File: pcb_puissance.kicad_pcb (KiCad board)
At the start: 2 copper layers, 126.5 x 120.5 mm, 32 parts, among them J1 1755736, J10 Conn_01x02, J11 Conn_01x02, J2 1755736, J3 1755736, J4 1755736, J5 1755736, J6 1755736, J7 1755736, J8 1755736, J9 Conn_01x02, K1 SRD-05VDC-SL-C

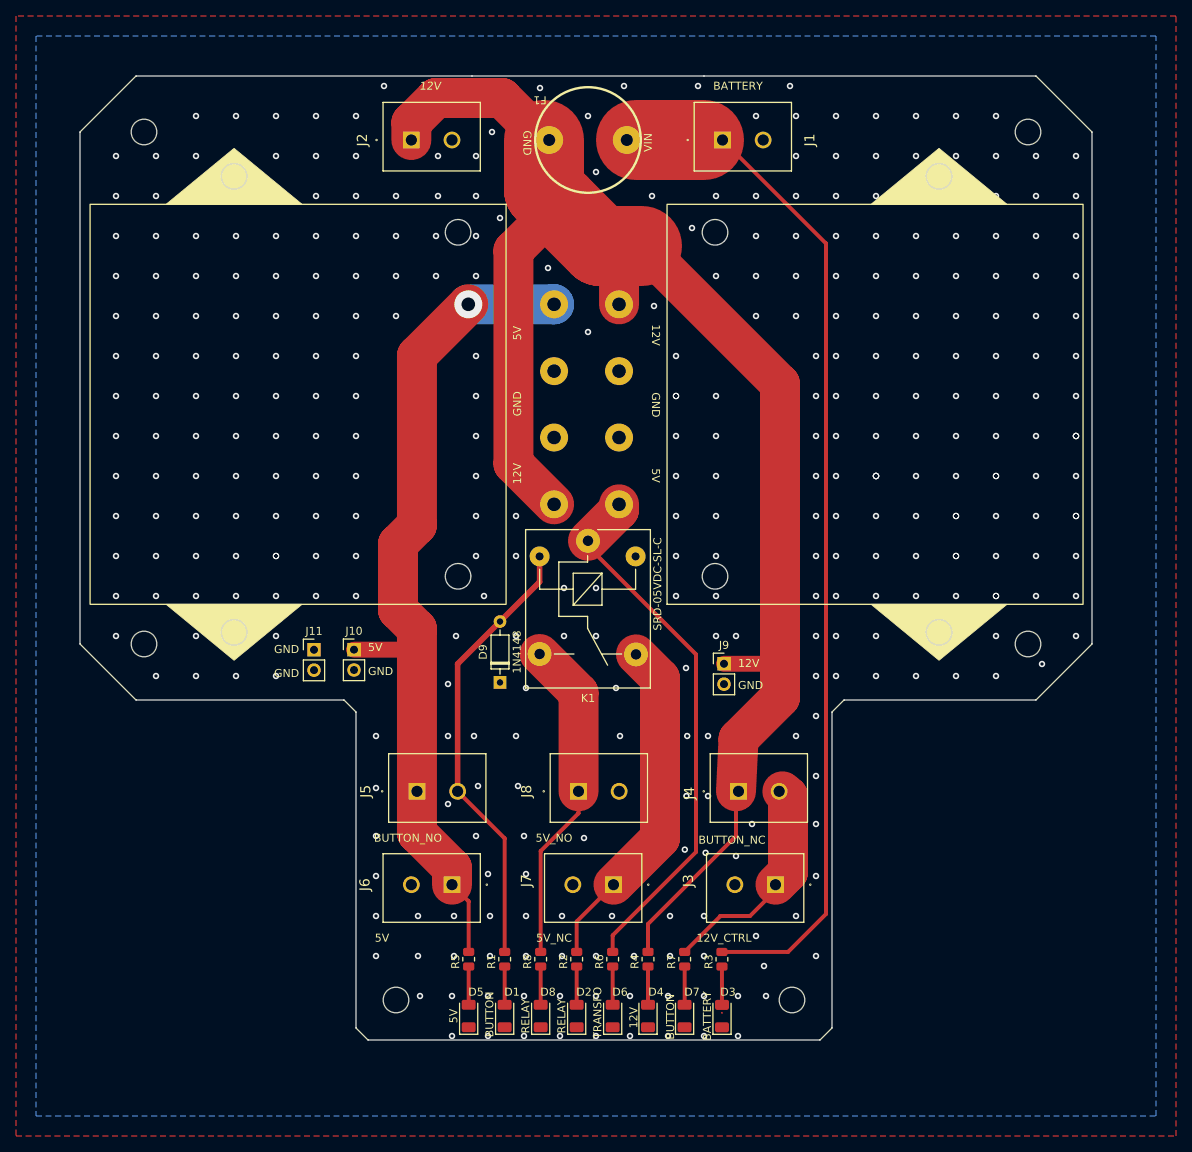
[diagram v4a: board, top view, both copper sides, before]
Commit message: Vias dans les pastilles + textes cachés par les connecteurs
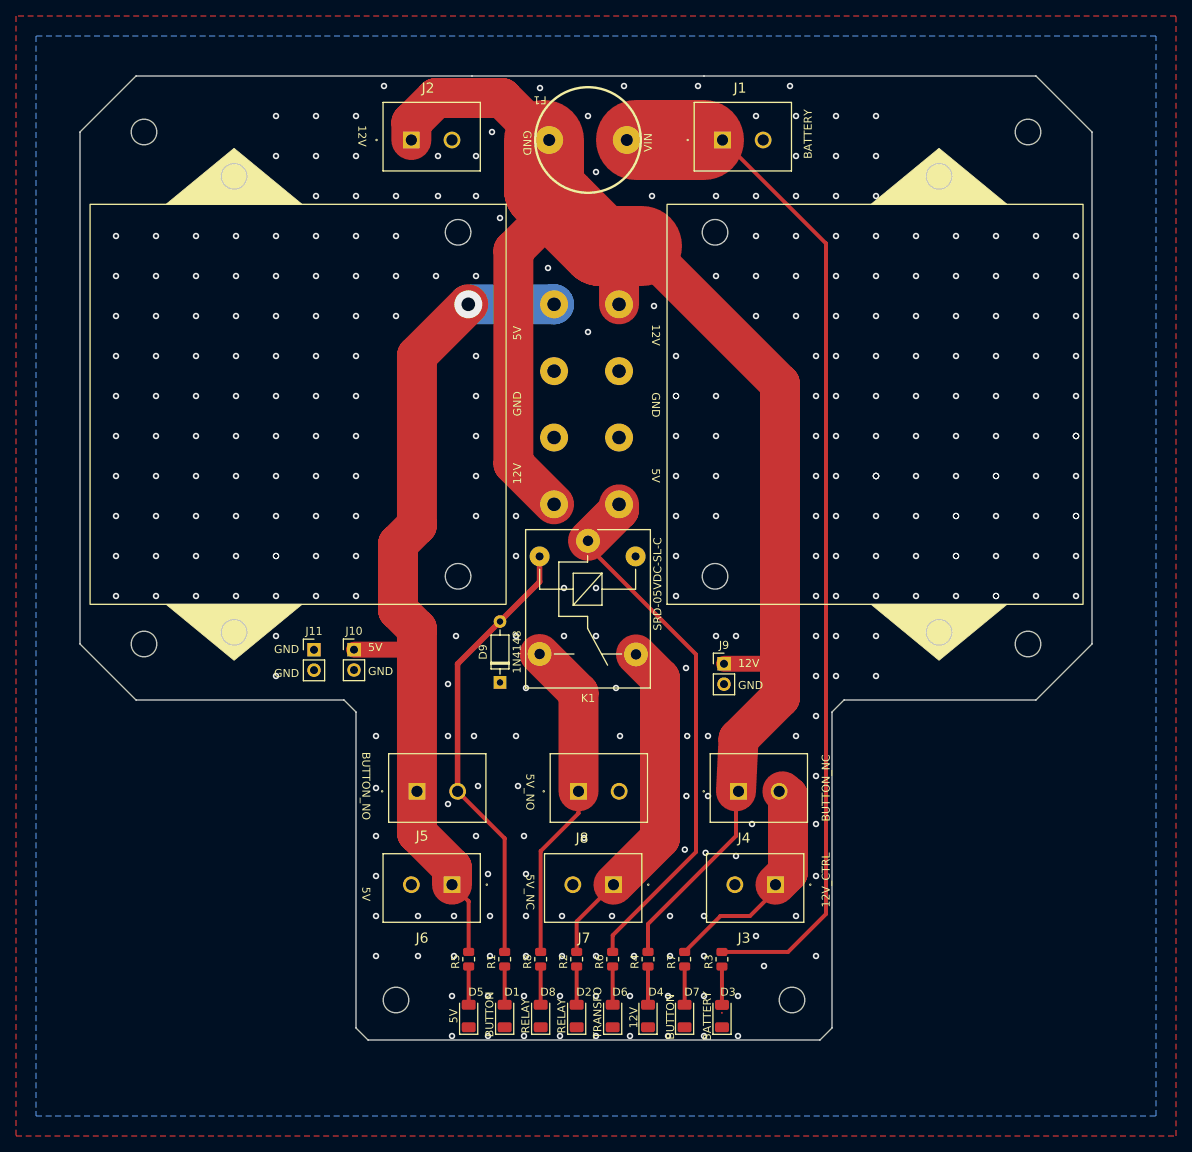
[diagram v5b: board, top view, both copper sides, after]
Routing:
- net GND: vias 361 -> 318

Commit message: Fixations
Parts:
- added Fix1: ~, Library:FIX3.2P7.5, F.Cu at (28.5, 32.0)
- added Fix2: ~, Library:FIX3.2P7.5, F.Cu at (139.0, 32.0)
- added Fix3: ~, Library:FIX3.2P7.5, F.Cu at (28.5, 96.0)
- added Fix4: ~, Library:FIX3.2P7.5, F.Cu at (139.0, 96.0)
- added Fix5: ~, Library:FIX3.2P7.5, F.Cu at (60.0, 140.5)
- added Fix6: ~, Library:FIX3.2P7.5, F.Cu at (109.5, 140.5)
- moved TRANSFO2 0.06 mm to (48.2, 66.0)
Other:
- outline, holes or cut-outs redrawn

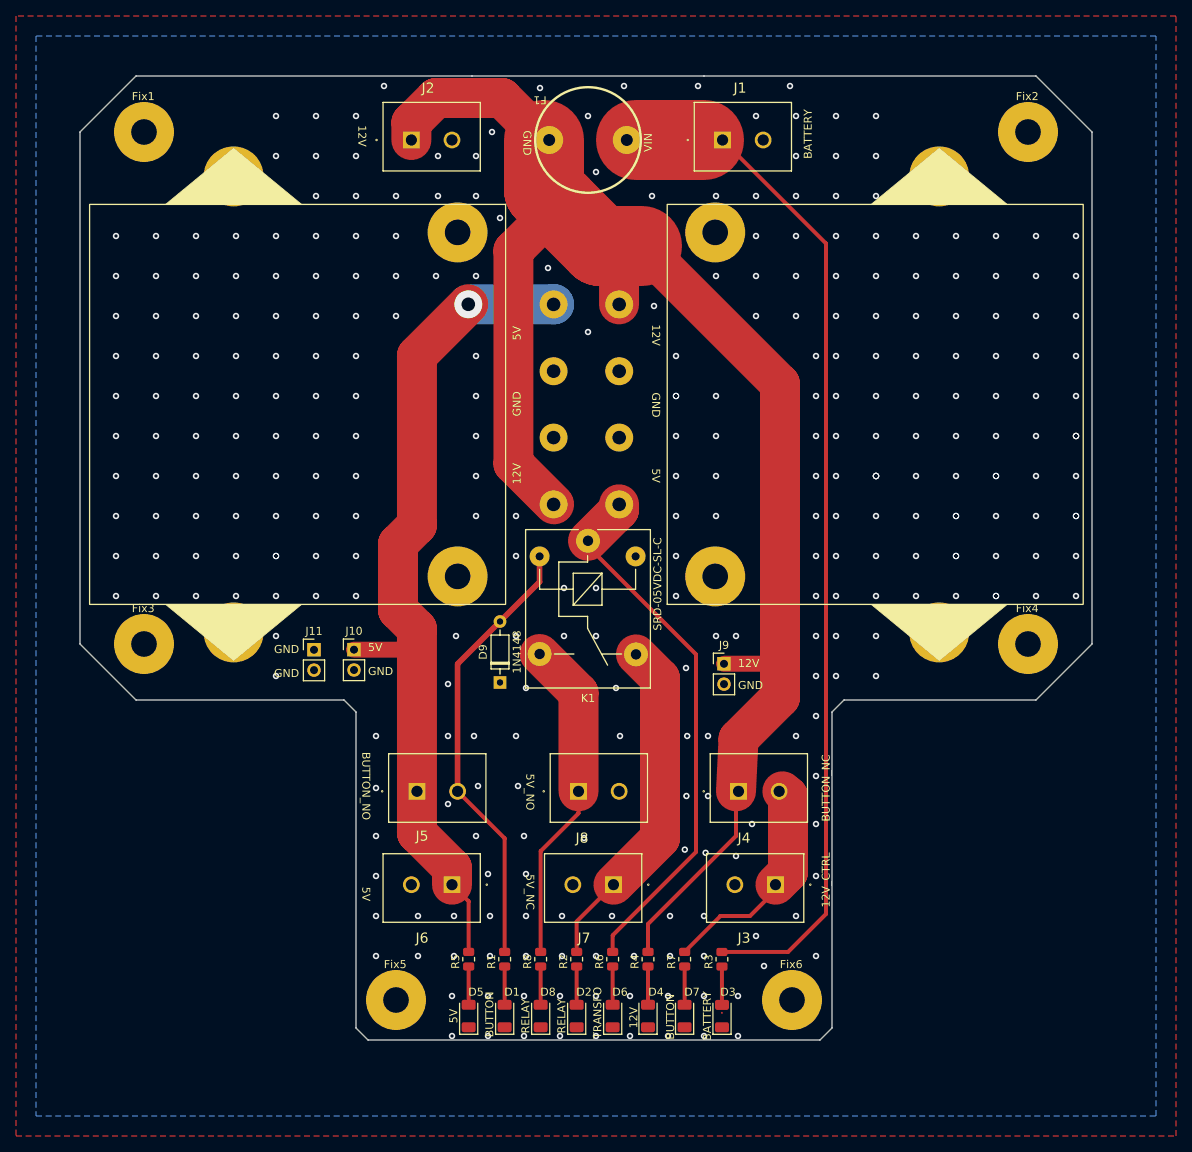
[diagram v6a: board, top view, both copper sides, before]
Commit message: DRC, nettoyage pistes cachées, ajout logos
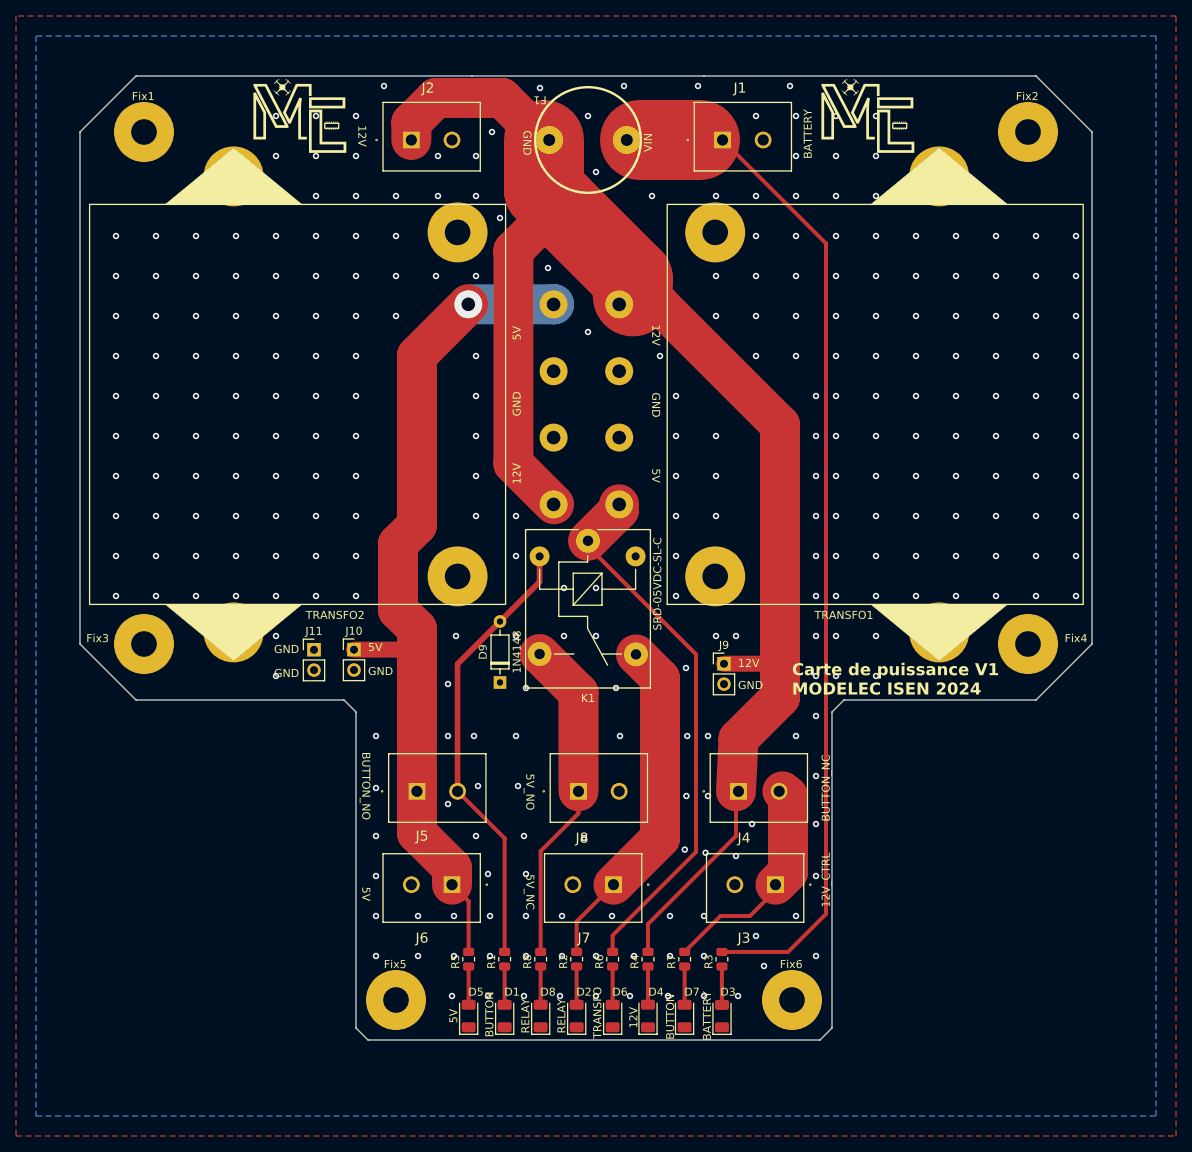
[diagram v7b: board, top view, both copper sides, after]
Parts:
- added G***: LOGO, Library:logo_modelec, F.Cu at (48.0, 30.0)
- added G***: LOGO, Library:logo_modelec, F.Cu at (119.0, 30.0)
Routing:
- net +12V: track 207.9 -> 196.9 mm
- net BATTERY: track 127.0 -> 124.6 mm
- net BUTTON_NC: track 27.9 -> 27.2 mm
- net GND: track 0.01 -> 0.00 mm, vias 318 -> 297
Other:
- board text added: "Carte de puissance V1 MODELEC ISEN 2024"
